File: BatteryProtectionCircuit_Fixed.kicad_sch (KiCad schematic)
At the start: 41 parts, among them J2 Conn_01x07_Pin, Q1 NMOS, U2 LM358, U3 LM358, U4 LM321, U6 LMC555xN

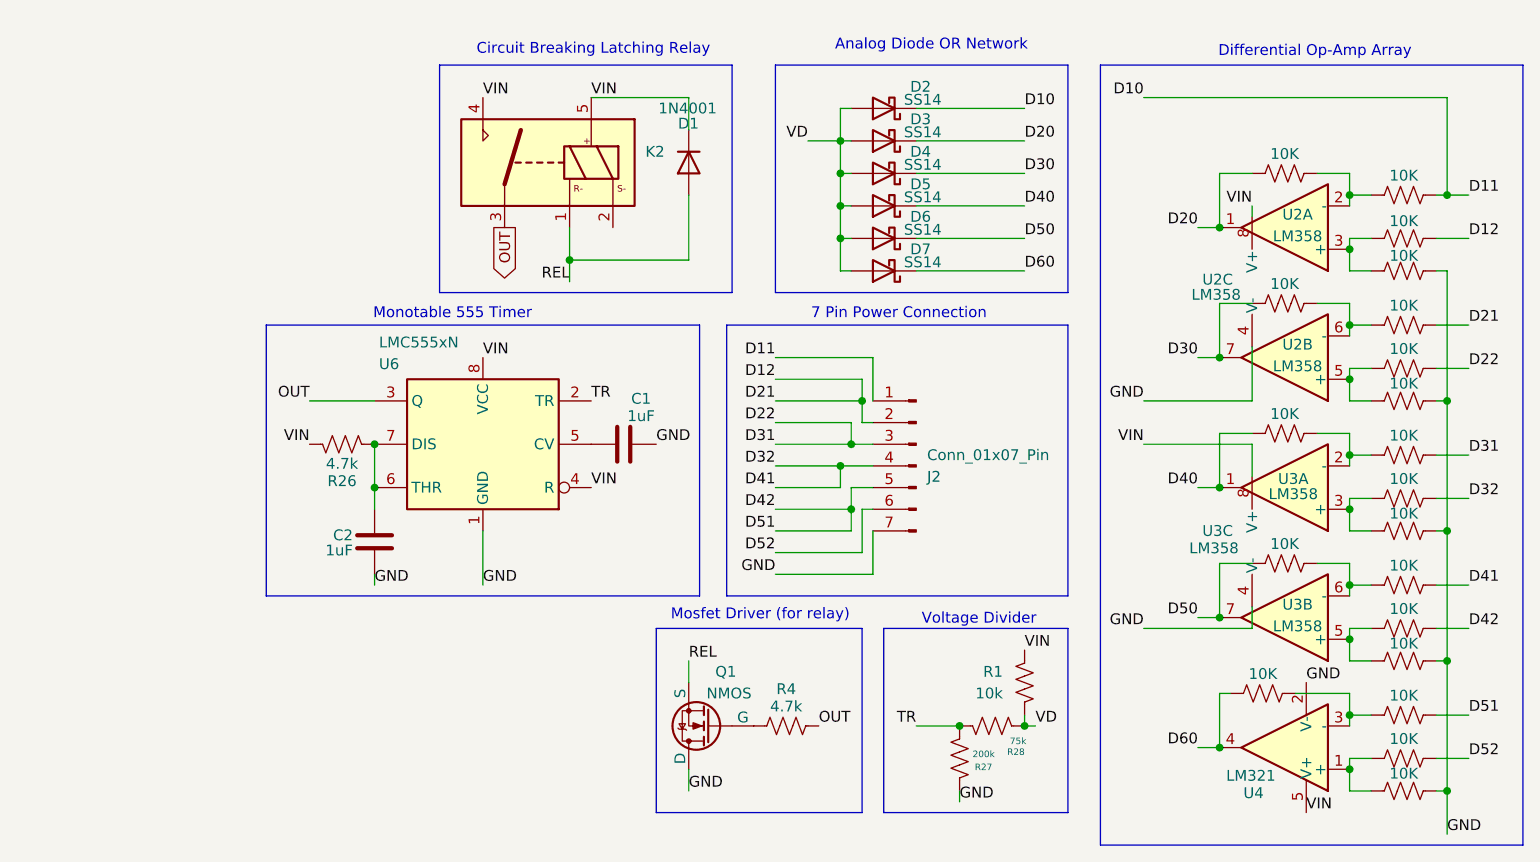
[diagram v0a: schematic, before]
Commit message: Added Connectors for power rail and robot input
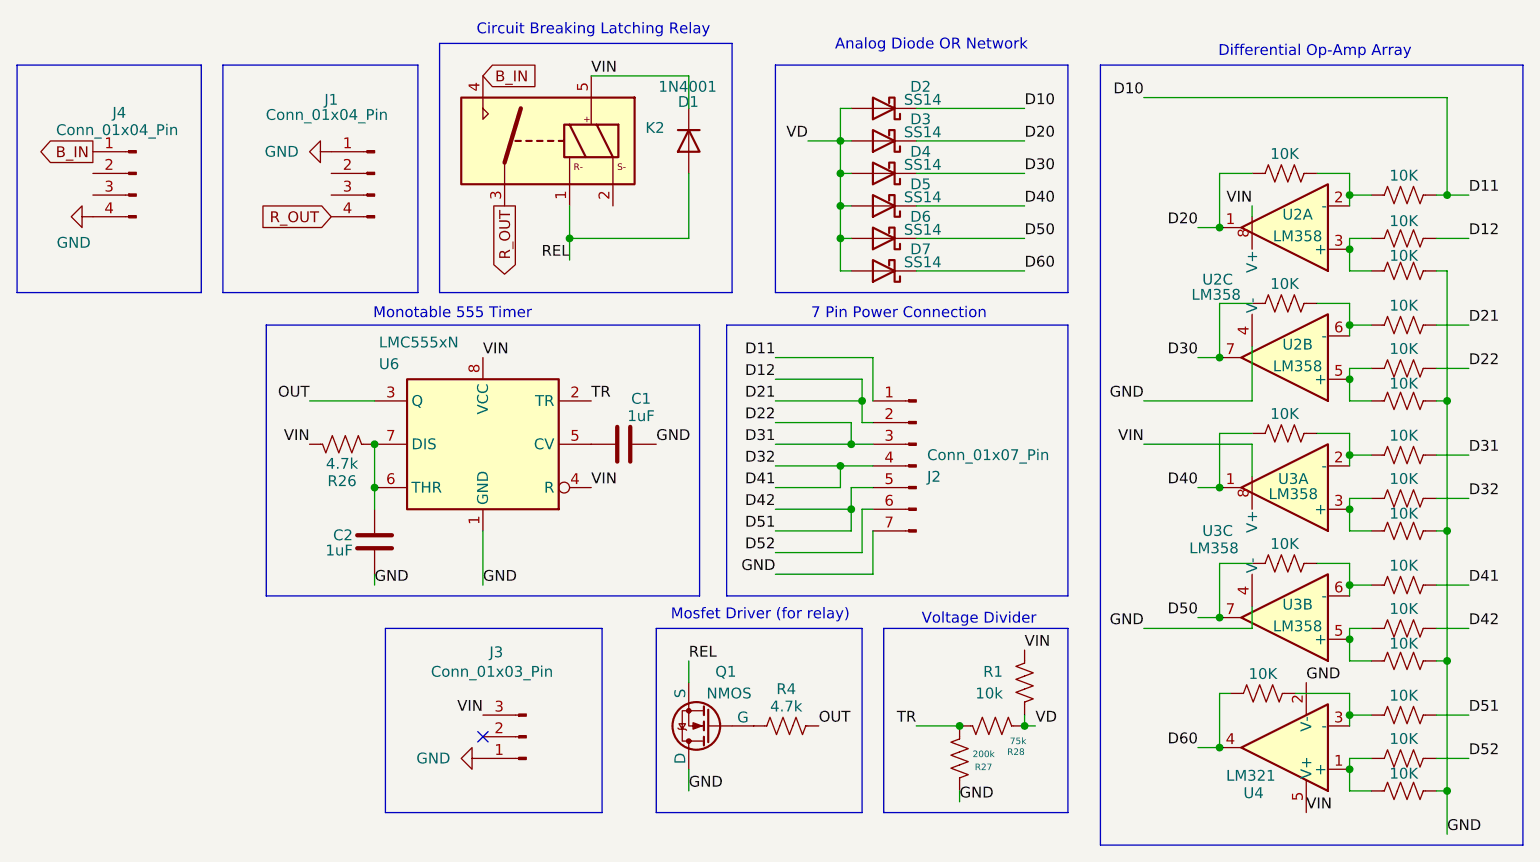
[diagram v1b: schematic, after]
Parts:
- added J1, J4: Conn_01x04_Pin, symbol Connector:Conn_01x04_Pin
- added J3: Conn_01x03_Pin, symbol Connector:Conn_01x03_Pin
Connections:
- net GND: now also J1.1 (Pin_1), J3.1 (Pin_1), J4.4 (Pin_4)
- net OUT: no longer K2.3
- net VIN: now also J3.3 (Pin_3); no longer K2.4
- new net B_IN: J4.1 (Pin_1), K2.4
- new net R_OUT: J1.4 (Pin_4), K2.3
- no-connect marks 0 -> 1
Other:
- moved on the sheet: D1, K2
